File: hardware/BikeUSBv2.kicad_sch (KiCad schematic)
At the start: 60 parts, among them J1 TYPE-C-31-M-16, J2 JST S2B-EH(LF)(SN), Q1 2SB772SQ, SW1 1TS002E-2500-2501-CT, SW2 1TS002E-2500-2501-CT, U1 TPS63070, U2 ATtiny1616-M, U3 FUSB302B10MPX, U4 HT7550, U5 TL431AIDBZR

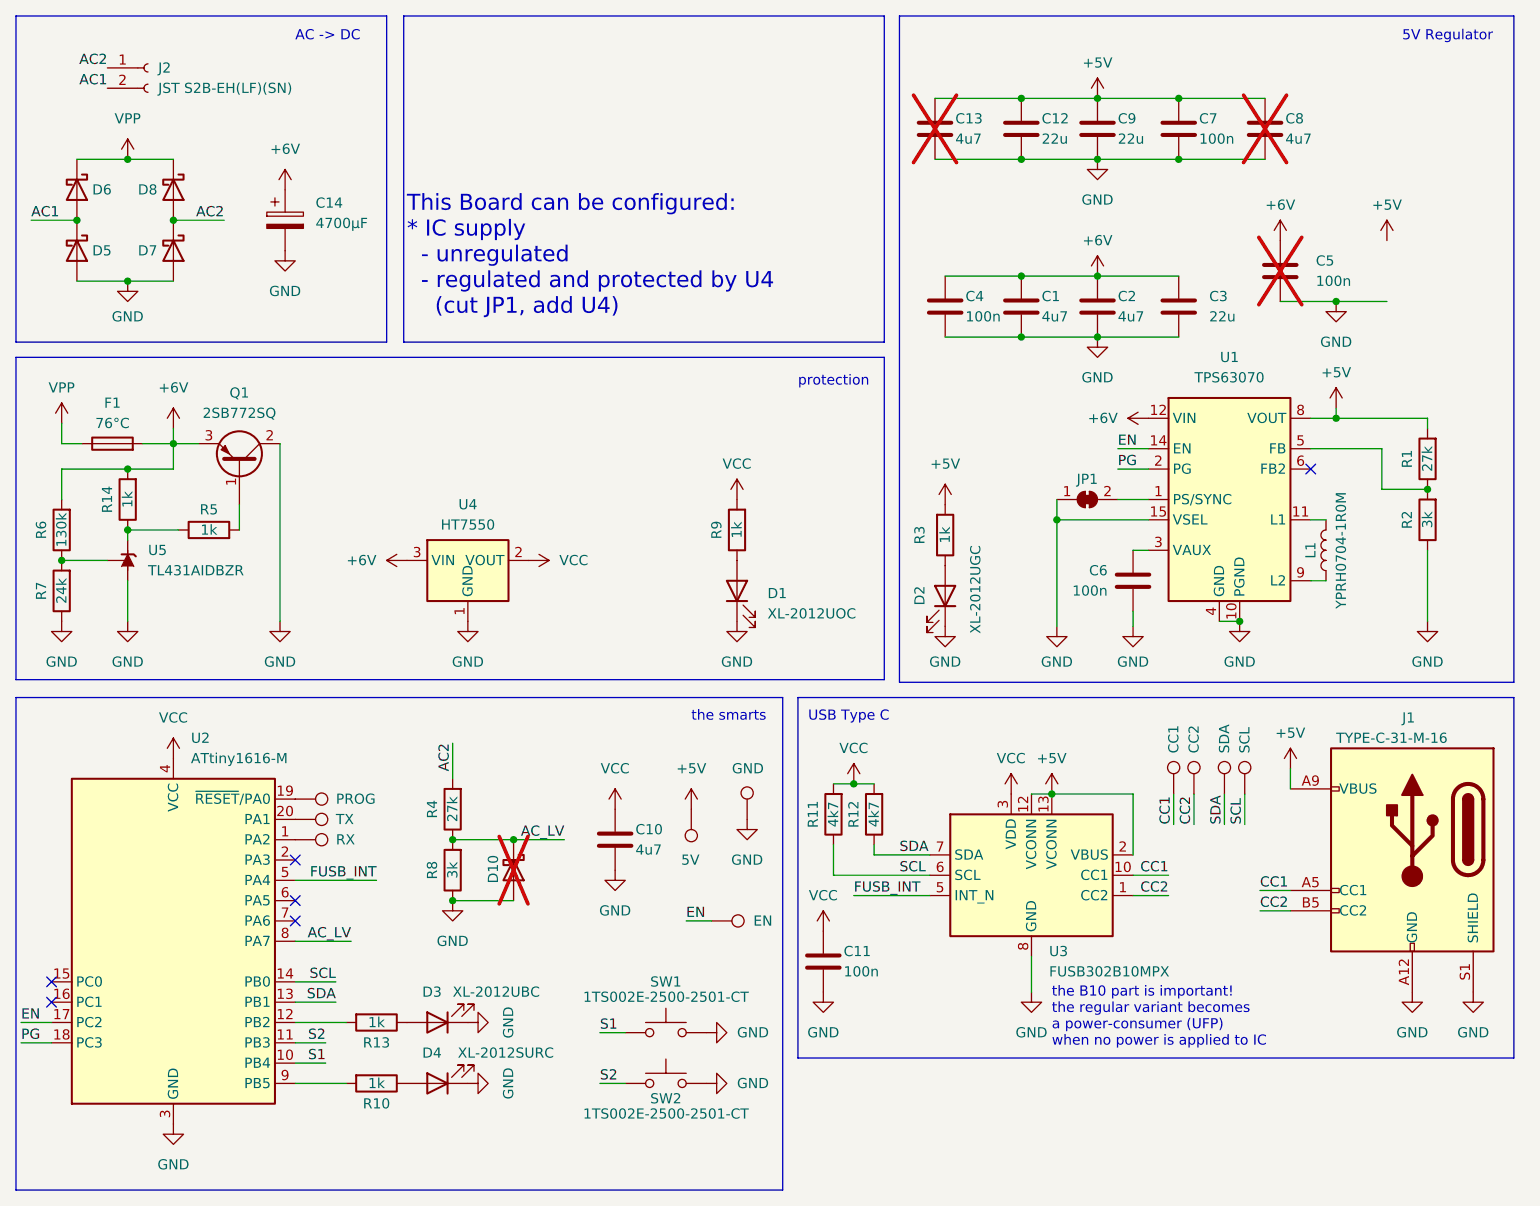
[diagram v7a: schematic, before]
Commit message: [PCB] silkscreen fixes and geographical reannotate
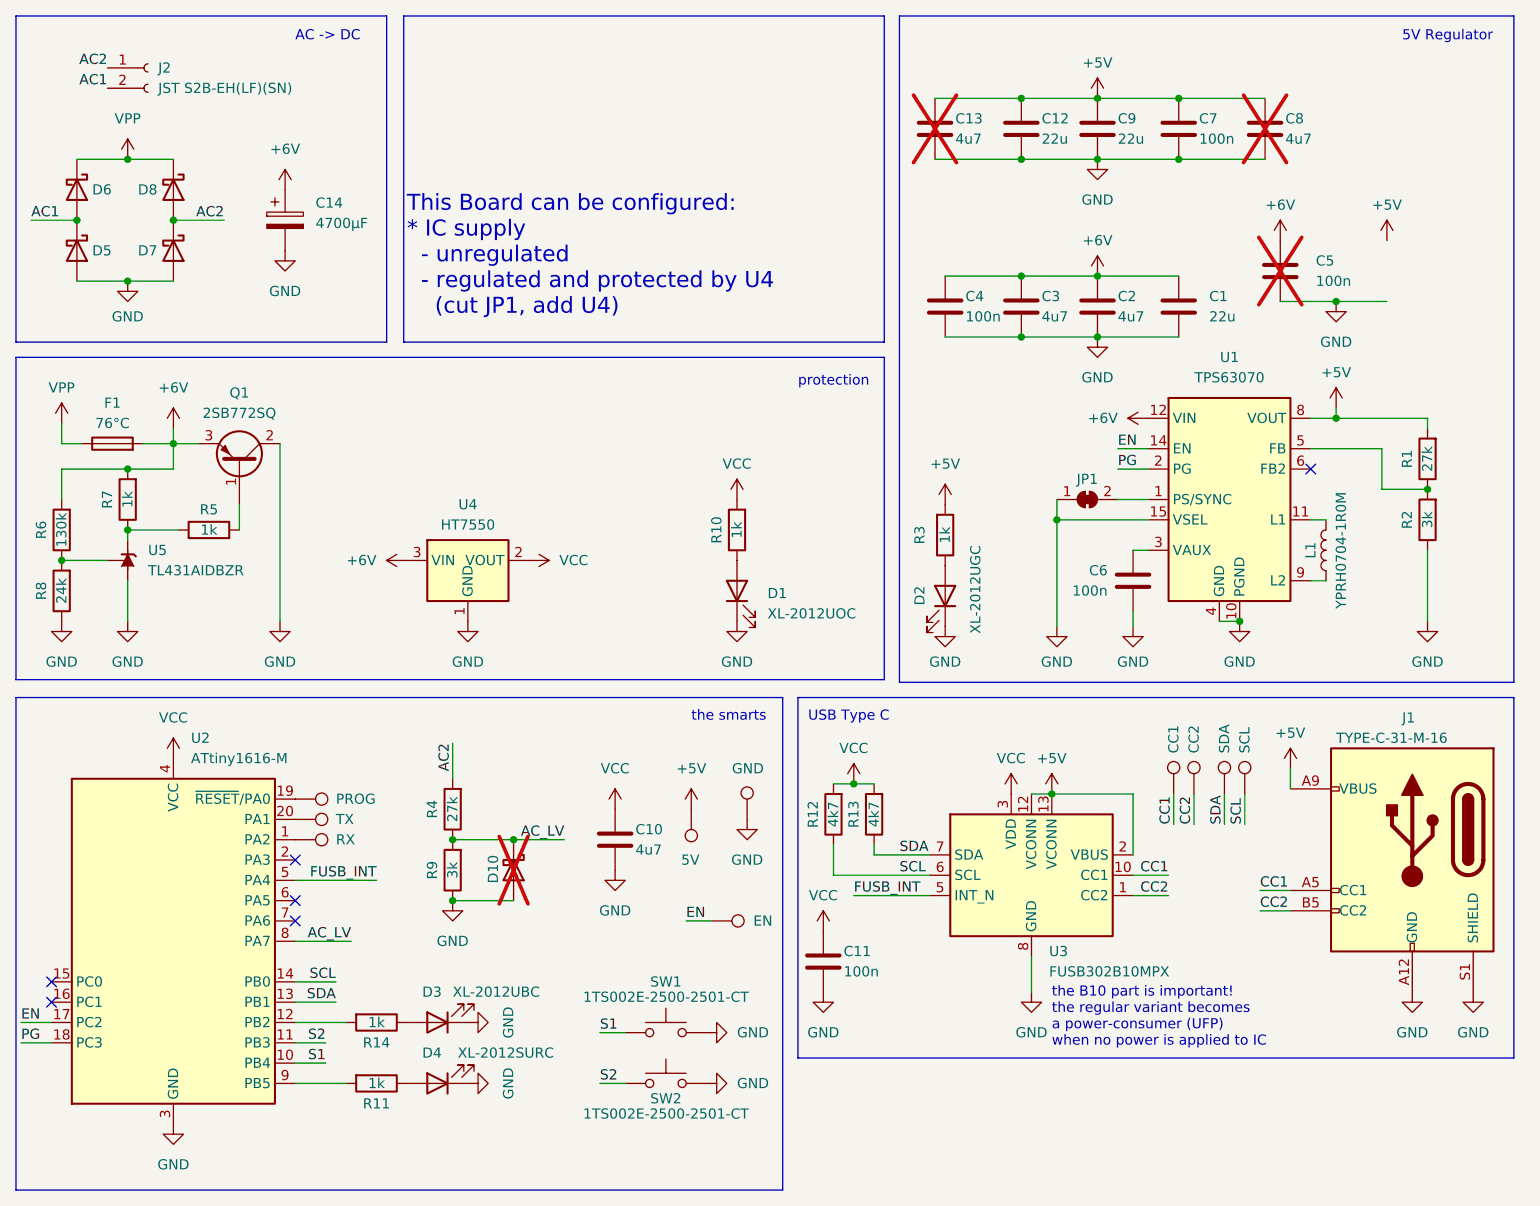
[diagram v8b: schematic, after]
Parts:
- renumbered C3 to C1, C1 to C3, R9 to R10, R10 to R11, R11 to R12, R12 to R13, R13 to R14, R14 to R7, R7 to R8, R8 to R9, TP6 to TP10, TP7 to TP6, TP8 to TP7, TP9 to TP8, TP10 to TP9
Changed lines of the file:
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@@
   (symbol (lib_id "Device:R") (at 106.68 81.28 180) (unit 1)
     (in_bom yes) (on_board yes) (dnp no)
-    (property "Reference" "R9" (at 104.14 81.28 90)
+    (property "Reference" "R10" (at 104.14 81.28 90)
       (effects (font (size 1.27 1.27)))
     )
@@
       (project "BikeUSBv2"
         (path "/b4aff538-5116-4944-9d24-c26a88d7dfe8"
-          (reference "R9") (unit 1)
+          (reference "R10") (unit 1)
         )
       )
@@
   (symbol (lib_id "Connector:TestPoint") (at 163.83 114.3 0) (unit 1)
     (in_bom no) (on_board yes) (dnp no)
-    (property "Reference" "TP8" (at 162.56 107.95 90)
+    (property "Reference" "TP7" (at 162.56 107.95 90)
       (effects (font (size 1.27 1.27)) (justify left) hide)
     )
@@
       (project "BikeUSBv2"
         (path "/b4aff538-5116-4944-9d24-c26a88d7dfe8"
-          (reference "TP8") (unit 1)
+          (reference "TP7") (unit 1)
         )
       )
@@
   (symbol (lib_id "Connector:TestPoint") (at 167.64 114.3 0) (unit 1)
     (in_bom no) (on_board yes) (dnp no)
-    (property "Reference" "TP9" (at 166.37 109.22 90)
+    (property "Reference" "TP8" (at 166.37 109.22 90)
       (effects (font (size 1.27 1.27)) (justify left) hide)
     )
@@
       (project "BikeUSBv2"
         (path "/b4aff538-5116-4944-9d24-c26a88d7dfe8"
-          (reference "TP9") (unit 1)
+          (reference "TP8") (unit 1)
         )
       )
@@
   (symbol (lib_id "Connector:TestPoint") (at 161.29 114.3 0) (unit 1)
     (in_bom no) (on_board yes) (dnp no)
-    (property "Reference" "TP7" (at 160.02 109.22 90)
+    (property "Reference" "TP6" (at 160.02 109.22 90)
       (effects (font (size 1.27 1.27)) (justify left) hide)
     )
@@
       (project "BikeUSBv2"
         (path "/b4aff538-5116-4944-9d24-c26a88d7dfe8"
-          (reference "TP7") (unit 1)
+          (reference "TP6") (unit 1)
         )
       )
@@
   (symbol (lib_id "Connector:TestPoint") (at 170.18 114.3 0) (unit 1)
     (in_bom no) (on_board yes) (dnp no)
-    (property "Reference" "TP10" (at 168.91 107.95 90)
+    (property "Reference" "TP9" (at 168.91 107.95 90)
       (effects (font (size 1.27 1.27)) (justify left) hide)
     )
@@
       (project "BikeUSBv2"
         (path "/b4aff538-5116-4944-9d24-c26a88d7dfe8"
-          (reference "TP10") (unit 1)
+          (reference "TP9") (unit 1)
         )
       )
@@
   (symbol (lib_id "Device:R") (at 118.745 116.84 180) (unit 1)
     (in_bom yes) (on_board yes) (dnp no)
-    (property "Reference" "R11" (at 116.205 116.84 90)
+    (property "Reference" "R12" (at 116.205 116.84 90)
       (effects (font (size 1.27 1.27)))
     )
@@
       (project "BikeUSBv2"
         (path "/b4aff538-5116-4944-9d24-c26a88d7dfe8"
-          (reference "R11") (unit 1)
+          (reference "R12") (unit 1)
         )
       )
@@
   (symbol (lib_id "Device:C") (at 161.925 53.34 0) (unit 1)
     (in_bom yes) (on_board yes) (dnp no) (fields_autoplaced)
-    (property "Reference" "C3" (at 165.735 52.07 0)
+    (property "Reference" "C1" (at 165.735 52.07 0)
       (effects (font (size 1.27 1.27)) (justify left))
     )
@@
       (project "BikeUSBv2"
         (path "/b4aff538-5116-4944-9d24-c26a88d7dfe8"
-          (reference "C3") (unit 1)
+          (reference "C1") (unit 1)
         )
       )
@@
   (symbol (lib_id "Device:R") (at 22.225 88.9 180) (unit 1)
     (in_bom yes) (on_board yes) (dnp no)
-    (property "Reference" "R7" (at 19.685 88.9 90)
+    (property "Reference" "R8" (at 19.685 88.9 90)
       (effects (font (size 1.27 1.27)))
     )
@@
       (project "BikeUSBv2"
         (path "/b4aff538-5116-4944-9d24-c26a88d7dfe8"
-          (reference "R7") (unit 1)
+          (reference "R8") (unit 1)
         )
       )
@@
   (symbol (lib_id "Device:R") (at 71.12 123.825 180) (unit 1)
     (in_bom yes) (on_board yes) (dnp no)
-    (property "Reference" "R8" (at 68.58 123.825 90)
+    (property "Reference" "R9" (at 68.58 123.825 90)
       (effects (font (size 1.27 1.27)))
     )
@@
       (project "BikeUSBv2"
         (path "/b4aff538-5116-4944-9d24-c26a88d7dfe8"
-          (reference "R8") (unit 1)
+          (reference "R9") (unit 1)
         )
       )
@@
   (symbol (lib_id "Device:R") (at 61.595 150.495 270) (unit 1)
     (in_bom yes) (on_board yes) (dnp no)
-    (property "Reference" "R10" (at 61.595 153.035 90)
+    (property "Reference" "R11" (at 61.595 153.035 90)
       (effects (font (size 1.27 1.27)))
     )
@@
       (project "BikeUSBv2"
         (path "/b4aff538-5116-4944-9d24-c26a88d7dfe8"
-          (reference "R10") (unit 1)
+          (reference "R11") (unit 1)
         )
       )
@@
   (symbol (lib_id "Connector:TestPoint") (at 51.435 120.015 270) (unit 1)
     (in_bom no) (on_board yes) (dnp no)
-    (property "Reference" "TP6" (at 57.785 118.745 90)
+    (property "Reference" "TP10" (at 57.785 118.745 90)
       (effects (font (size 1.27 1.27)) (justify left) hide)
     )
@@
       (project "BikeUSBv2"
         (path "/b4aff538-5116-4944-9d24-c26a88d7dfe8"
-          (reference "TP6") (unit 1)
+          (reference "TP10") (unit 1)
         )
       )
@@
   (symbol (lib_id "Device:R") (at 61.595 142.875 270) (unit 1)
     (in_bom yes) (on_board yes) (dnp no)
-    (property "Reference" "R13" (at 61.595 145.415 90)
+    (property "Reference" "R14" (at 61.595 145.415 90)
       (effects (font (size 1.27 1.27)))
     )
@@
       (project "BikeUSBv2"
         (path "/b4aff538-5116-4944-9d24-c26a88d7dfe8"
-          (reference "R13") (unit 1)
+          (reference "R14") (unit 1)
         )
       )
@@
   (symbol (lib_id "Device:C") (at 142.24 53.34 0) (unit 1)
     (in_bom yes) (on_board yes) (dnp no)
-    (property "Reference" "C1" (at 144.78 52.07 0)
+    (property "Reference" "C3" (at 144.78 52.07 0)
       (effects (font (size 1.27 1.27)) (justify left))
     )
@@
       (project "BikeUSBv2"
         (path "/b4aff538-5116-4944-9d24-c26a88d7dfe8"
-          (reference "C1") (unit 1)
+          (reference "C3") (unit 1)
         )
       )
@@
   (symbol (lib_id "Device:R") (at 123.825 116.84 180) (unit 1)
     (in_bom yes) (on_board yes) (dnp no)
-    (property "Reference" "R12" (at 121.285 116.84 90)
+    (property "Reference" "R13" (at 121.285 116.84 90)
       (effects (font (size 1.27 1.27)))
     )
@@
       (project "BikeUSBv2"
         (path "/b4aff538-5116-4944-9d24-c26a88d7dfe8"
-          (reference "R12") (unit 1)
+          (reference "R13") (unit 1)
         )
       )
@@
   (symbol (lib_id "Device:R") (at 30.48 77.47 180) (unit 1)
     (in_bom yes) (on_board yes) (dnp no)
-    (property "Reference" "R14" (at 27.94 77.47 90)
+    (property "Reference" "R7" (at 27.94 77.47 90)
       (effects (font (size 1.27 1.27)))
     )
@@
       (project "BikeUSBv2"
         (path "/b4aff538-5116-4944-9d24-c26a88d7dfe8"
-          (reference "R14") (unit 1)
-        )
-      )
+          (reference "R7") (unit 1)
+        )
+      )
